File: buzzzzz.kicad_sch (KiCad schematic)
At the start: 0 parts

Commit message: I THIHK I GET IT NOW
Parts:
- added C70: 10u, Capacitor_SMD:C_0805_2012Metric, symbol Device:C
- added C71: 0.1u, Capacitor_SMD:C_0603_1608Metric, symbol Device:C
- added D17: 1N5819HW-7-F, charger_parts:1N5819HW-7-F, symbol Device:D_Schottky
- added Q9: IRLML0030TRPBF, charger_parts:IRLML0030TRPBF, symbol IRLML0030TRPBF:IRLML0030TRPBF
- added R57: 100k, Resistor_SMD:R_0603_1608Metric, symbol Device:R
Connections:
- new net +14V: C70.1, C71.1, D17.1 (K)
- new net BUZ-: D17.2 (A), Q9.3 (D)
- new net BuzzPWM: Q9.1 (G), R57.2
- new net GND: C70.2, C71.2, Q9.2 (S), R57.1
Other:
- note added: "BUZZZZZZZZZZZZZZZZ"

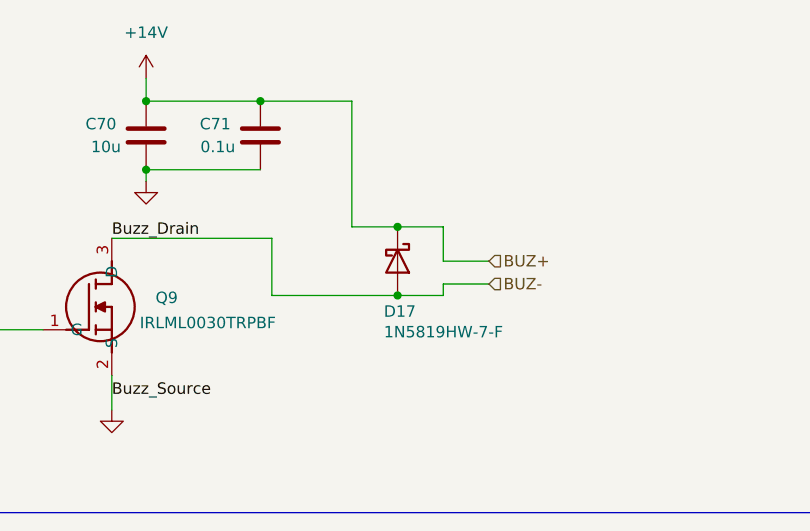
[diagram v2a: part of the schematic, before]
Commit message: i will fix the stupid pins on the mcu schem later
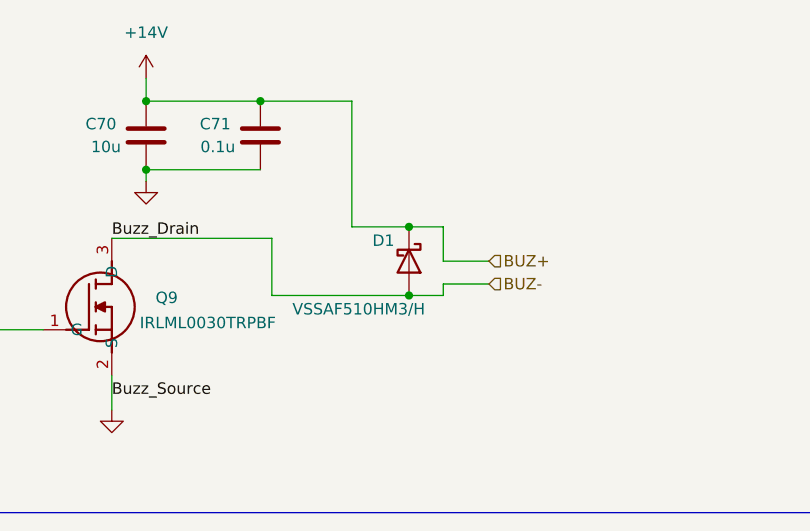
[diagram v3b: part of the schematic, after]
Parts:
- removed D17: 1N5819HW-7-F, charger_parts:1N5819HW-7-F, symbol Device:D_Schottky
- added D1: VSSAF510HM3/H, symbol Device:D_Schottky
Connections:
- net +14V: now also D1.1 (K)
- net BUZ-: now also D1.2 (A)
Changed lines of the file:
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@@
 	)
 	(junction
-		(at 114.3 44.45)
-		(diameter 0)
-		(color 0 0 0 0)
-	)
-	(junction
-		(at 114.3 52.07)
+		(at 115.57 52.07)
 		(diameter 0)
 		(color 0 0 0 0)
@@
 	)
 	(junction
+		(at 115.57 44.45)
+		(diameter 0)
+		(color 0 0 0 0)
+	)
+	(junction
 		(at 46.99 55.88)
 		(diameter 0)
@@
 	(wire
 		(pts
-			(xy 114.3 44.45) (xy 119.38 44.45)
-		)
-		(stroke
-			(width 0)
-			(type default)
-		)
-	)
-	(wire
-		(pts
 			(xy 119.38 44.45) (xy 119.38 48.26)
 		)
@@
 	(wire
 		(pts
-			(xy 114.3 52.07) (xy 119.38 52.07)
-		)
-		(stroke
-			(width 0)
-			(type default)
-		)
-	)
-	(wire
-		(pts
 			(xy 119.38 50.8) (xy 119.38 52.07)
 		)
@@
 	(wire
 		(pts
+			(xy 115.57 44.45) (xy 119.38 44.45)
+		)
+		(stroke
+			(width 0)
+			(type default)
+		)
+	)
+	(wire
+		(pts
+			(xy 115.57 52.07) (xy 119.38 52.07)
+		)
+		(stroke
+			(width 0)
+			(type default)
+		)
+	)
+	(wire
+		(pts
 			(xy 46.99 55.88) (xy 74.93 55.88)
 		)
@@
 	(wire
 		(pts
-			(xy 100.33 52.07) (xy 114.3 52.07)
-		)
-		(stroke
-			(width 0)
-			(type default)
-		)
-	)
-	(wire
-		(pts
-			(xy 109.22 44.45) (xy 114.3 44.45)
+			(xy 100.33 52.07) (xy 115.57 52.07)
+		)
+		(stroke
+			(width 0)
+			(type default)
+		)
+	)
+	(wire
+		(pts
+			(xy 109.22 44.45) (xy 115.57 44.45)
 		)
 		(stroke
@@
 			)
 			(justify right)
-		)
-	)
-	(symbol
-		(lib_name "D_Schottky_1")
-		(lib_id "Device:D_Schottky")
-		(at 114.3 48.26 270)
-		(unit 1)
-		(body_style 1)
-		(exclude_from_sim no)
-		(in_bom yes)
-		(on_board yes)
-		(in_pos_files yes)
-		(dnp no)
-		(property "Reference" "D17"
-			(at 112.776 53.848 90)
-			(show_name no)
-			(do_not_autoplace no)
-			(effects
-				(font
-					(size 1.27 1.27)
-				)
-				(justify left)
-			)
-		)
-		(property "Value" "1N5819HW-7-F"
-			(at 112.776 56.134 90)
-			(show_name no)
-			(do_not_autoplace no)
-			(effects
-				(font
-					(size 1.27 1.27)
-				)
-				(justify left)
-			)
-		)
-		(property "Footprint" "charger_parts:1N5819HW-7-F"
-			(at 16.84 59.69 0)
-			(hide yes)
-			(show_name no)
-			(do_not_autoplace no)
-			(effects
-				(font
-					(size 1.27 1.27)
-				)
-				(justify left top)
-			)
-		)
-		(property "Datasheet" "https://www.diodes.com//assets/Datasheets/1N5819HW.pdf"
-			(at -83.16 59.69 0)
-			(hide yes)
-			(show_name no)
-			(do_not_autoplace no)
-			(effects
-				(font
-					(size 1.27 1.27)
-				)
-				(justify left top)
-			)
-		)
-		(property "Description" "Diode Schottky 1A 40V SOD123 Diodes Inc 1N5819HW-7-F, SMT Schottky Diode, 40V 1A, 2-Pin SOD-123"
-			(at 114.3 48.26 0)
-			(hide yes)
-			(show_name no)
-			(do_not_autoplace no)
-			(effects
-				(font
-					(size 1.27 1.27)
-				)
-			)
-		)
-		(property "Height" "1.45"
-			(at -283.16 59.69 0)
-			(hide yes)
-			(show_name no)
-			(do_not_autoplace no)
-			(effects
-				(font
-					(size 1.27 1.27)
-				)
-				(justify left top)
-			)
-		)
-		(property "Mouser Part Number" "621-1N5819HW-F"
-			(at -383.16 59.69 0)
-			(hide yes)
-			(show_name no)
-			(do_not_autoplace no)
-			(effects
-				(font
-					(size 1.27 1.27)
-				)
-				(justify left top)
-			)
-		)
-		(property "Mouser Price/Stock" "https://www.mouser.co.uk/ProductDetail/Diodes-Incorporated/1N5819HW-7-F?qs=NQ47qNm99eDyWTEd07miYA%3D%3D"
-			(at -483.16 59.69 0)
-			(hide yes)
-			(show_name no)
-			(do_not_autoplace no)
-			(effects
-				(font
-					(size 1.27 1.27)
-				)
-				(justify left top)
-			)
-		)
-		(property "Manufacturer_Name" "Diodes Incorporated"
-			(at -583.16 59.69 0)
-			(hide yes)
-			(show_name no)
-			(do_not_autoplace no)
-			(effects
-				(font
-					(size 1.27 1.27)
-				)
-				(justify left top)
-			)
-		)
-		(property "Manufacturer_Part_Number" "1N5819HW-7-F"
-			(at -683.16 59.69 0)
-			(hide yes)
-			(show_name no)
-			(do_not_autoplace no)
-			(effects
-				(font
-					(size 1.27 1.27)
-				)
-				(justify left top)
-			)
-		)
-		(property "P/N" "1N5819HW-7-F"
-			(at 114.3 48.26 90)
-			(hide yes)
-			(show_name no)
-			(do_not_autoplace no)
-			(effects
-				(font
-					(size 1.27 1.27)
-				)
-			)
-		)
-		(pin "2"
-		)
-		(pin "1"
-		)
-		(instances
-			(project "atempt_2"
-				(path "/86244622-fc6f-4400-a6c8-ba7d84e5ad42/cc50543f-c5a2-400d-8754-d6e2a0f4c571"
-					(reference "D17")
-					(unit 1)
-				)
-			)
-			(project "PS-ChargerInterfacePCB"
-				(path "/894adbd2-6316-426a-afb4-88808e8ec51a/cc50543f-c5a2-400d-8754-d6e2a0f4c571"
-					(reference "D17")
-					(unit 1)
-				)
-			)
 		)
 	)
@@
 					(unit 1)
 				)
+			)
+		)
+	)
+	(symbol
+		(lib_id "Device:D_Schottky")
+		(at 115.57 48.26 270)
+		(unit 1)
+		(body_style 1)
+		(exclude_from_sim no)
+		(in_bom yes)
+		(on_board yes)
+		(in_pos_files yes)
+		(dnp no)
+		(property "Reference" "D1"
+			(at 111.506 45.974 90)
+			(show_name no)
+			(do_not_autoplace no)
+			(effects
+				(font
+					(size 1.27 1.27)
+				)
+				(justify left)
+			)
+		)
+		(property "Value" "VSSAF510HM3/H"
+			(at 102.616 53.594 90)
+			(show_name no)
+			(do_not_autoplace no)
+			(effects
+				(font
+					(size 1.27 1.27)
+				)
+				(justify left)
+			)
+		)
+		(property "Footprint" ""
+			(at 115.57 48.26 0)
+			(hide yes)
+			(show_name no)
+			(do_not_autoplace no)
+			(effects
+				(font
+					(size 1.27 1.27)
+				)
+			)
+		)
+		(property "Datasheet" ""
+			(at 115.57 48.26 0)
+			(hide yes)
+			(show_name no)
+			(do_not_autoplace no)
+			(effects
+				(font
+					(size 1.27 1.27)
+				)
+			)
+		)
+		(property "Description" "Schottky diode"
+			(at 115.57 48.26 0)
+			(hide yes)
+			(show_name no)
+			(do_not_autoplace no)
+			(effects
+				(font
+					(size 1.27 1.27)
+				)
+			)
+		)
+		(pin "2"
+		)
+		(pin "1"
+		)
+		(instances
+			(project "PS-ChargerInterfacePCB"
+				(path "/894adbd2-6316-426a-afb4-88808e8ec51a/cc50543f-c5a2-400d-8754-d6e2a0f4c571"
+					(reference "D1")
+					(unit 1)
+				)

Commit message: updated from review
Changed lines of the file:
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@@
-		)
-	)
-	(label "Buzz_Drain"
-		(at 82.55 45.72 0)
-		(effects
-			(font
-				(size 1.27 1.27)
-			)
-			(justify left bottom)
-		)
-	)
-	(label "Buzz_Source"
-		(at 82.55 63.5 0)
-		(effects
-			(font
-				(size 1.27 1.27)
-			)
-			(justify left bottom)
 		)
 	)
@@
 		)
 	)
+	(hierarchical_label "Buzz_Source"
+		(shape input)
+		(at 82.55 63.5 180)
+		(effects
+			(font
+				(size 1.27 1.27)
+			)
+			(justify right)
+		)
+	)
+	(hierarchical_label "Buzz_Drain"
+		(shape input)
+		(at 82.55 45.72 180)
+		(effects
+			(font
+				(size 1.27 1.27)
+			)
+			(justify right)
+		)
+	)
